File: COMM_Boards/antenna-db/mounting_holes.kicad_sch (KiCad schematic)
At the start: 20 parts

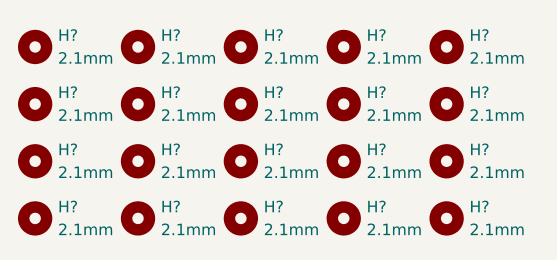
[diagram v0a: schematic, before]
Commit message: COMM: antt-dbd: map mounting holes to pcb layout
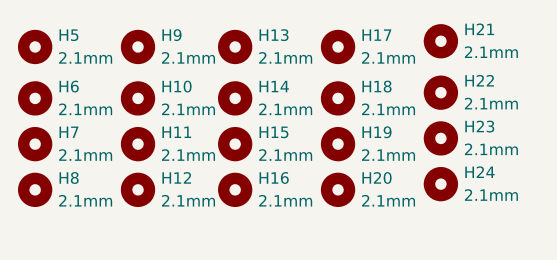
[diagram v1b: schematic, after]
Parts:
- removed H? (x19): 2.1mm, symbol Mechanical:MountingHole
- added H10, H11, H12, H13, H14, H15, H16, H17, H18, H19, H20, H21, H22, H23, H24, H6, H7, H8, H9: 2.1mm, MountingHole:MountingHole_2.2mm_M2_Pad_TopBottom, symbol Mechanical:MountingHole
- H5: renamed from H?; footprint (none) -> MountingHole:MountingHole_2.2mm_M2_Pad_TopBottom

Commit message: COMM: antt-dbd: finish deployment detection and arming control
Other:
- company: (none) -> Queen's Space Engineering Team - Satellite
- title: (none) -> Antenna Deployment Board
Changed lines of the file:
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@@
 (kicad_sch (version 20211123) (generator eeschema)
   (paper "A4")
+  (title_block
+    (title "Antenna Deployment Board")
+    (date "2023-04-24")
+    (rev "RevA")
+    (company "Queen's Space Engineering Team - Satellite")
+  )
   (symbol (lib_id "Mechanical:MountingHole") (at 81.28 85.725 0) (unit 1)
     (in_bom yes) (on_board yes) (fields_autoplaced)
